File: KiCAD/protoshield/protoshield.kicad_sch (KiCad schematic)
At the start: 1 part, among them U2 Metro_ESP32S3

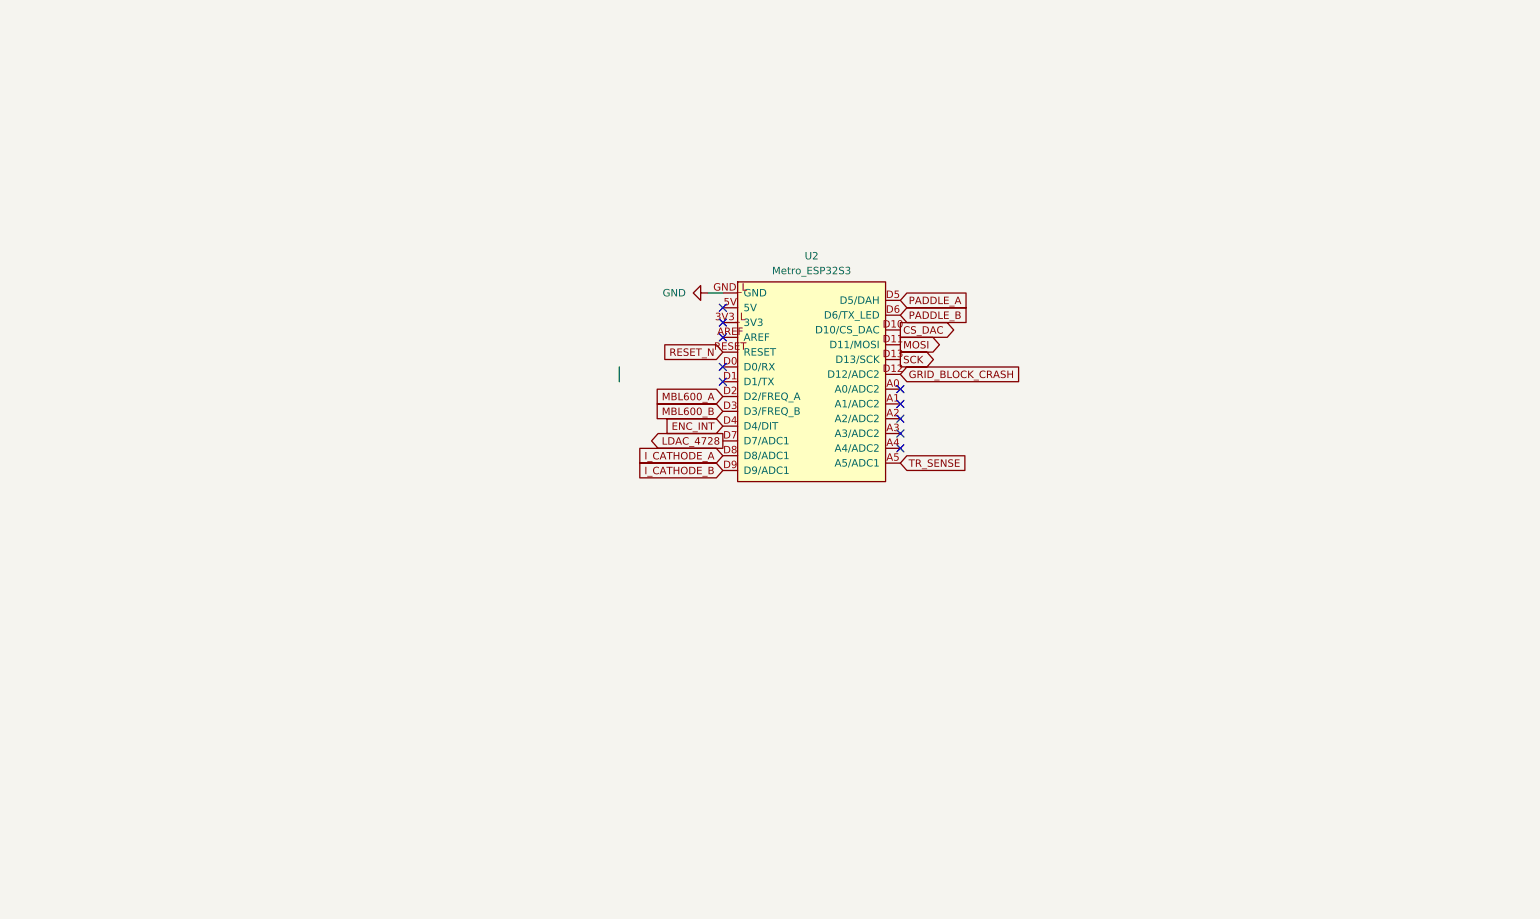
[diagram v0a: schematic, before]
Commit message: KiCad revB: protoshield schematic complete + 1N4728A symbol + misc board edits
Protoshield (Metro ESP32-S3 GPIO signal conditioning):
- Full schematic drawn: series R + bypass C + Zener clamp for I_CATHODE_A/B
  (1k+100nF+1N4728A), MBL600_A/B (10k/20k divider + 22pF), GRID_BLOCK_CRASH
  (1k+100nF), ENC_INT (330R+10k pull-up), PADDLE_A/B (10k pull-ups), RESET_N
  (100nF), TR_SENSE (10k pull-up), passthrough nodes for SPI and LDAC_4728
- All THT footprints assigned (ceramic disc caps, DIN0207 resistors, Phoenix
  MKDS-1.5 2-pin/3-pin terminal blocks)
- ENC_INT wiring gap fixed (R7 re-placed to connect J4 pin 2 to ENC_INT net)
- sym-lib-table added (points to shared xmitter.kicad_sym)
- protoshield.net generated netlist added for reference

Symbol library (xmitter.kicad_sym):
- Added 1N4728A (3.3V 1W Zener, DO-41) with correct KiCad 9.0 inline pts format

Other boards:
- analog/arduino.kicad_sch: minor junction/reference adjustments after Metro
  symbol was removed to protoshield in prior session
- bias: kicad_pro and kicad_sch updated (ongoing schematic work)
- power/sym-lib-table added for new stub project

Added: Purchase Orders (JLCPCB + Digi-Key invoices), tools/_scan_symbols.py

Co-Authored-By: Claude Sonnet 4.6 <noreply@anthropic.com>
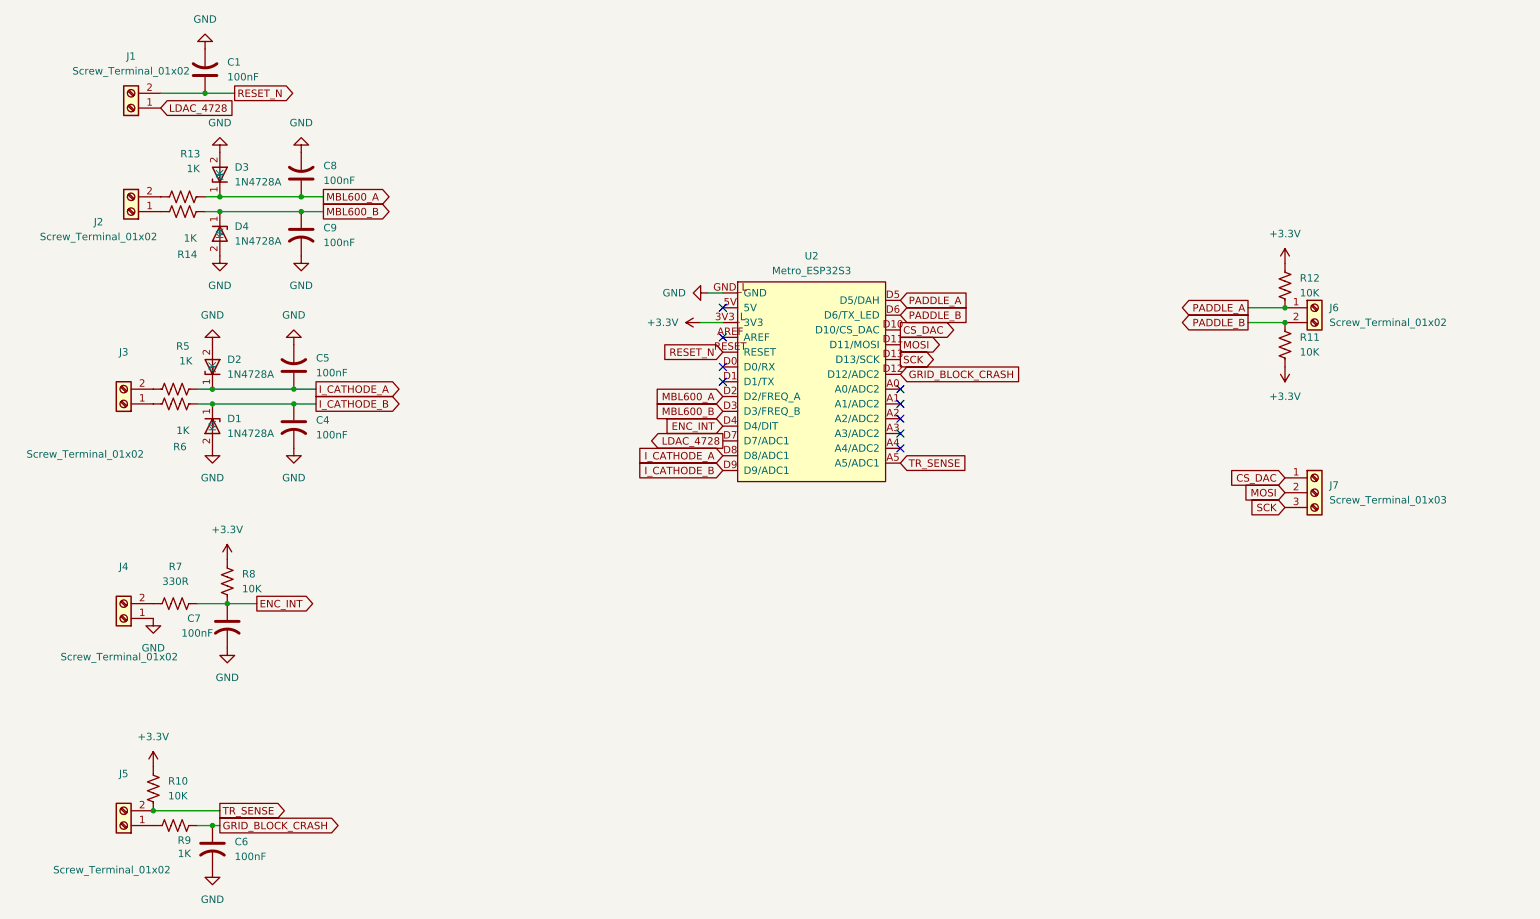
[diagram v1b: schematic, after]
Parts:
- added C1, C4, C5, C6, C7, C8, C9: 100nF, Capacitor_THT:C_Disc_D5.0mm_W2.5mm_P2.50mm, symbol Device:C_US
- added D1, D2, D3, D4: 1N4728A, Diode_THT:D_DO-41_SOD81_P10.16mm_Horizontal, symbol xmitter:1N4728A
- added J1, J2, J3, J4, J5, J6: Screw_Terminal_01x02, TerminalBlock_Phoenix:TerminalBlock_Phoenix_MKDS-1,5-2_1x02_P5.00mm_Horizontal, symbol Connector:Screw_Terminal_01x02
- added J7: Screw_Terminal_01x03, TerminalBlock_Phoenix:TerminalBlock_Phoenix_MKDS-1,5-3_1x03_P5.00mm_Horizontal, symbol Connector:Screw_Terminal_01x03
- added R10, R11, R12, R8: 10K, Resistor_THT:R_Axial_DIN0207_L6.3mm_D2.5mm_P10.16mm_Horizontal, symbol Device:R_US
- added R13, R14, R5, R6, R9: 1K, Resistor_THT:R_Axial_DIN0207_L6.3mm_D2.5mm_P10.16mm_Horizontal, symbol Device:R_US
- added R7: 330R, Resistor_THT:R_Axial_DIN0207_L6.3mm_D2.5mm_P10.16mm_Horizontal, symbol Device:R_US
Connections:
- net CS_DAC: now also J7.1 (Pin_1)
- net ENC_INT: now also C7.1, R7.2, R8.2
- net GND: now also C1.2, C4.2, C5.2, C6.2, C7.2, C8.2, C9.2, D1.2 (A), D2.2 (A), D3.2 (A), D4.2 (A), J4.1 (Pin_1)
- net GRID_BLOCK_CRASH: now also C6.1, R9.2
- net I_CATHODE_A: now also C5.1, D2.1 (K), R5.2
- net I_CATHODE_B: now also C4.1, D1.1 (K), R6.2
- net LDAC_4728: now also J1.1 (Pin_1)
- net MBL600_A: now also C8.1, D3.1 (K), R13.2
- net MBL600_B: now also C9.1, D4.1 (K), R14.2
- net MOSI: now also J7.2 (Pin_2)
- net PADDLE_A: now also J6.1 (Pin_1), R12.2
- net PADDLE_B: now also J6.2 (Pin_2), R11.1
- net RESET_N: now also C1.1, J1.2 (Pin_2)
- net SCK: now also J7.3 (Pin_3)
- net TR_SENSE: now also J5.2 (Pin_2), R10.2
- net +3.3V: now reaches U2.3V3_L (3V3)
- net +3.3V: now also R10.1, R11.2, R12.1, R8.1
- new net: J4.2 (Pin_2), R7.1
- new net: J2.2 (Pin_2), R13.1
- new net: J3.1 (Pin_1), R6.1
- new net: J3.2 (Pin_2), R5.1
- new net: J2.1 (Pin_1), R14.1
- new net: J5.1 (Pin_1), R9.1
- no-connect marks 10 -> 9

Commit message: KiCad revB: schematic review pass — I2C, ENC_INT, GND returns, GRID_BLOCK_CRASH clamp
Result of extended review pass against fresh netlists across all four
boards. All connectivity blockers resolved.

- Si5351 SDA/SCL wired via 0R jumpers (R8/R9) puts I2C on PCB traces
  for PCF8575 U17 and the RJ45 to the front panel. MCP4728 side has
  parallel 0R jumpers (R3/R4/R5) left DNP by default — STEMMA-QT is
  the intended path.
- ENC_INT chain unified end-to-end with staged names:
  ENC_INT_RAW (frontpanel encoder wire-OR) → ENC_INT_CLEAN (across
  CAT + analog pass-through) → ENC_INT_FINAL (post-protoshield
  conditioning). Frontpanel U4 (MCP1700-3.3 LDO) sources the +3.3V
  the pull-up R4 needs; pull-up moved to encoder side for sharper
  falling edges over the 2 m CAT run.
- Protoshield GRID_BLOCK_CRASH gets 1N4728A Zener clamp (D5),
  matching the I_CATHODE and MBL600 5V→3.3V clamp topology.
- Protoshield MBL600 conditioning rebuilt: 1K series + 100nF filter
  + 1N4728A clamp (was 10K/20K divider + 22pF that filtered nothing
  below RF).
- PADDLE_A/B and RESET_N removed from analog board — case-mounted
  switches wire directly to protoshield.
- Protoshield J1/J6 widened to 3-pin to include GND returns for the
  case-mounted paddle and reset switches.
- Bias board reference designators reorganized functionally
  (R_FA/R_FB feedback, R_GA/R_GB gain, R_PADA/R_PADB, R_GLA/R_GLB
  grid line, R_GATE, R_Z).
- New Documentation/control_board_functional_blocks.md captures
  KeyUp/Gate 2 keying, relay assignments (J6=T/R, J7=HV primary,
  J8=HV inrush), CD14538B heartbeat watchdog, TR_SENSE interlock,
  and J13 power-migration header.
- Fresh netlists exported for all four boards.

Co-Authored-By: Claude Opus 4.7 <noreply@anthropic.com>
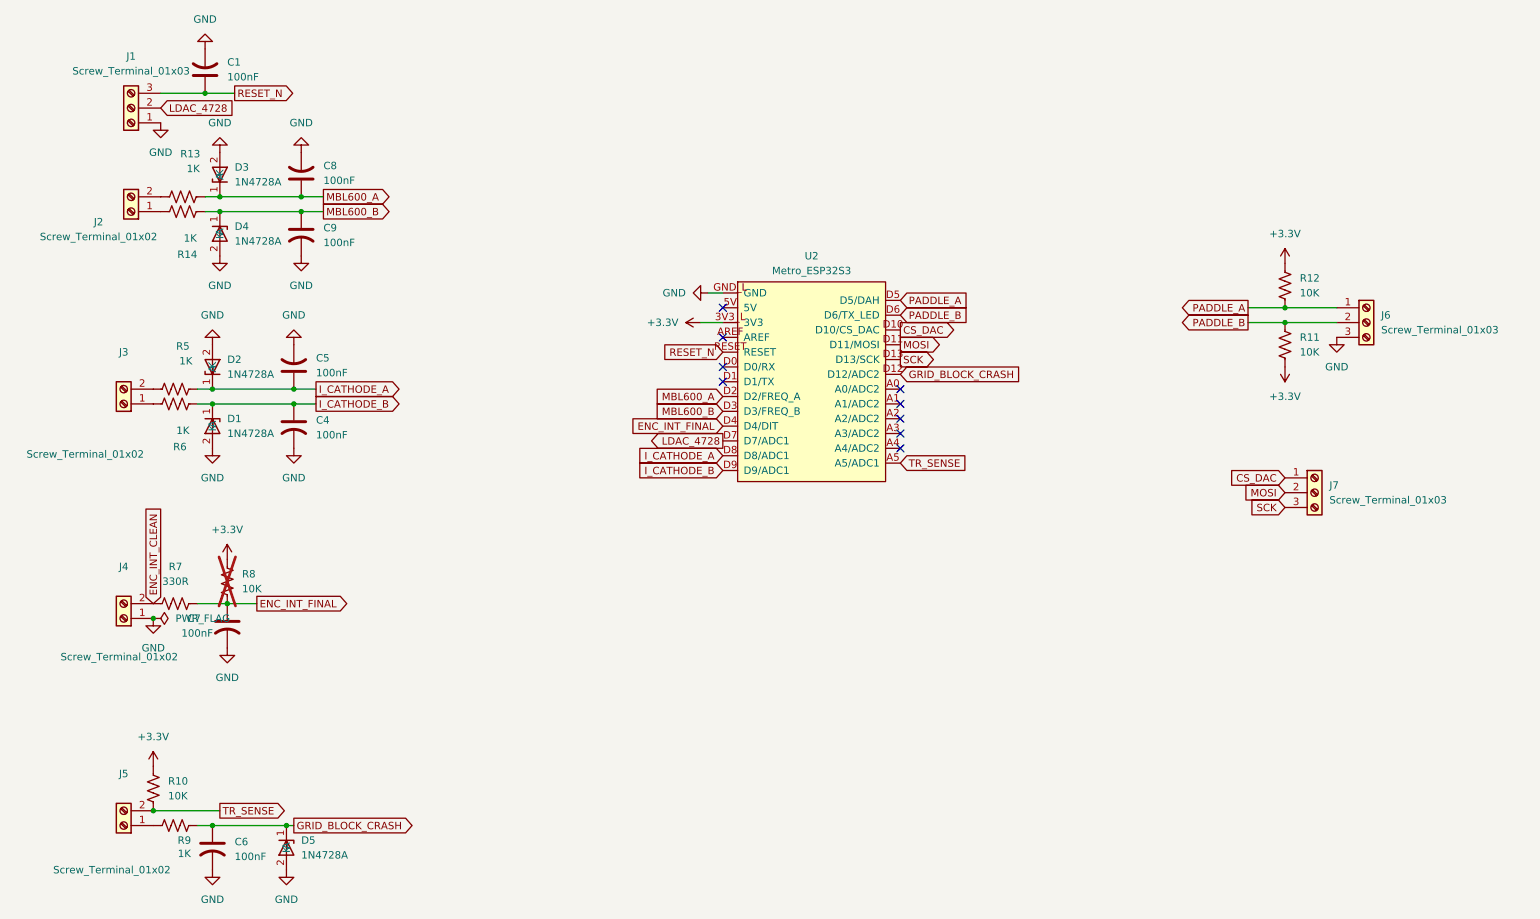
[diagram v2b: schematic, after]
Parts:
- removed J1, J6: Screw_Terminal_01x02, TerminalBlock_Phoenix:TerminalBlock_Phoenix_MKDS-1,5-2_1x02_P5.00mm_Horizontal, symbol Connector:Screw_Terminal_01x02
- added D5: 1N4728A, Diode_THT:D_DO-41_SOD81_P10.16mm_Horizontal, symbol xmitter:1N4728A
- added J1, J6: Screw_Terminal_01x03, symbol Connector:Screw_Terminal_01x03
- R8: now not fitted
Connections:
- net GND: now also D5.2 (A), J1.1 (Pin_1), J6.3 (Pin_3)
- net GRID_BLOCK_CRASH: now also D5.1 (K)
- net LDAC_4728: now also J1.2 (Pin_2)
- net PADDLE_A: now also J6.1 (Pin_1)
- net PADDLE_B: now also J6.2 (Pin_2)
- net RESET_N: now also J1.3 (Pin_3)
- net ENC_INT_CLEAN: now reaches J4.2 (Pin_2), R7.1
- net ENC_INT renamed ENC_INT_FINAL

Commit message: KiCad revB: assign 87 empty footprints via re-runnable scripts
Filled empty Footprint fields on capacitors, resistors, and screw
terminals across all four boards. All three scripts are re-runnable
and only fill empty fields (never overwrite existing assignments).

Scripts:
- assign_cap_footprints.py: extended CAP_LIB_IDS to also cover
  Device:C_US, Device:C_Polarized_US, Device:C_Small (was only
  Device:C and Device:C_Polarized). VALUE_TO_FOOTPRINT map unchanged.
- assign_connector_footprints.py (new): matches
  Connector:Screw_Terminal_01xNN to Phoenix MKDS-1,5-N horizontal
  P5.00mm per pin count (same pattern the protoshield already used).
- assign_resistor_footprints.py (new): matches Device:R and
  Device:R_US to the project-standard Resistor_THT:R_Axial_DIN0207
  L6.3mm_D2.5mm_P10.16mm_Horizontal footprint. All 46 populated
  resistors on the project already used this footprint; the empty
  ones now match.

Assignment counts:
- Capacitors: 42 (5 arduino, 33 vfo_complete, 2 bias, 2 frontpanel)
- Screw terminals: 17 (10 arduino, 4 bias, 1 frontpanel, 2 protoshield)
- Resistors: 28 (5 arduino, 21 vfo_complete, 2 frontpanel)

Deferred (need part-specific decisions, tracked in review notes):
- Coax connectors (12 total across analog + bias) - awaiting Cinch
  142-0701-201 footprint verification in KiCad's Connector_Coaxial
  library, or a custom footprint in xmitter.pretty/
- One-off ICs: F1 Polyfuse, U3 MCP4728, U21 LT1054
- 6 unmapped cap values in vfo_complete: 2pF x3, 220nF, 4700uF, 100uF
- U2 Metro_ESP32S3 (protoshield): intentionally empty (on_board no,
  plug-in module, not placed on PCB)

Also add three component datasheets: 1N4736AT-D (1N4728A family
reference), LM393-D, OPA1641.

Co-Authored-By: Claude Opus 4.7 <noreply@anthropic.com>
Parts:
- J1, J6: footprint (none) -> TerminalBlock_Phoenix:TerminalBlock_Phoenix_MKDS-1,5-3_1x03_P5.00mm_Horizontal
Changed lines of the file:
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@@
 			)
 		)
-		(property "Footprint" ""
+		(property "Footprint" "TerminalBlock_Phoenix:TerminalBlock_Phoenix_MKDS-1,5-3_1x03_P5.00mm_Horizontal"
 			(at 241.3 74.93 0)
 			(hide yes)
@@
 			)
 		)
-		(property "Footprint" ""
+		(property "Footprint" "TerminalBlock_Phoenix:TerminalBlock_Phoenix_MKDS-1,5-3_1x03_P5.00mm_Horizontal"
 			(at 29.21 38.1 0)
 			(hide yes)

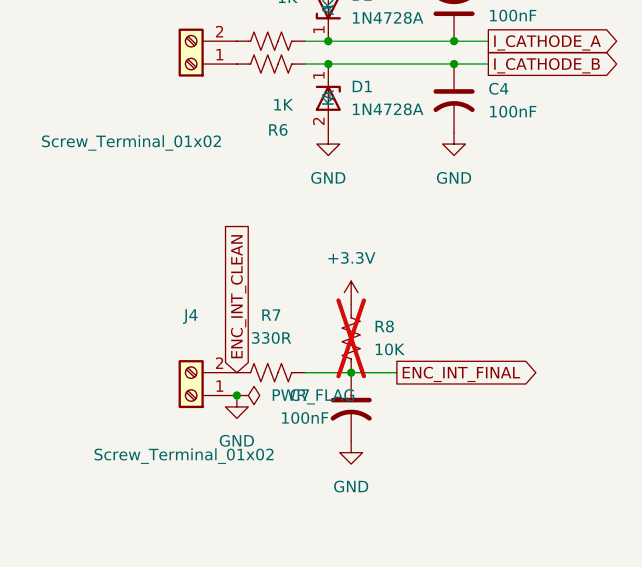
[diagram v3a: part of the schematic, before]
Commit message: KiCad revB: custom footprints, coax assignments, TO-92 widening, ENC_INT rewire
Second-pass footprint work: filled the remaining empty footprints
that couldn't be handled by the earlier stock-library scripts, added
custom footprints for parts KiCad's stock library doesn't cover, and
did a few schematic hygiene fixes surfaced during the deep-dive
reviews.

Custom footprints (new, xmitter.pretty/):
- SMA_Cinch_142-0701-201_Vertical_JackPCB - 50 Ohm SMA vertical
  through-hole jack for the analog board and bias board coax
  interconnects (I_CATHODE, GRID_CTL, GRID_BLOCK_CRASH, GRID_BIAS).
  Center pin 1.57 mm hole + 4 ground tabs on a 5.08 mm square
  pattern. All 4 ground tabs share pin number 2 (shield).
- CP_Radial_Kemet_ESK_D22.0mm_P10.00mm - Kemet ESK case Q4 radial
  electrolytic (22 mm dia, 10 mm pitch) for C72 = 4700 uF 50V.
- Fuse_Littelfuse_60R_L7.9mm_W3.1mm_P5.08mm - Littelfuse 60R Series
  radial polyfuse for F1 = 60R050XU (0.5 A hold). Body sized for the
  small-body variants (010X-090X); pitch 5.08 mm, drill 0.7 mm.
- C_Axial_Kemet_Aximax_C41X_L4.5mm_D2.6mm_P7.62mm_Horizontal - Kemet
  Aximax C410 axial C0G ceramic for the three 2 pF caps
  (C69/C70/C71) in the vfo_complete keyer chain. Horizontal mount,
  7.62 mm pitch.

New re-runnable script:
- tools/assign_coax_footprints.py - maps
  Connector:Conn_Coaxial_Small symbols to the new Cinch SMA
  footprint. Same "only fill empty, never overwrite" pattern as the
  existing assign_*_footprints.py scripts.

Script extension:
- tools/assign_cap_footprints.py - added value entries for 4700uF
  (Kemet ESK), 220nF (D6 disc), 2pF (Kemet Aximax C41X), and 100uF
  (Vishay 036 RSP). All four entries include the datasheet path and
  the specific case-size rationale.

Schematic edits (all boards):
- 12 coax connectors assigned to the new Cinch SMA footprint
  (analog J17-J19/J23-J24, bias J1/J2/J4/J6/J9/J10/J12) via the new
  assign_coax script.
- 5 caps in vfo_complete assigned via extended assign_cap_footprints
  (C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
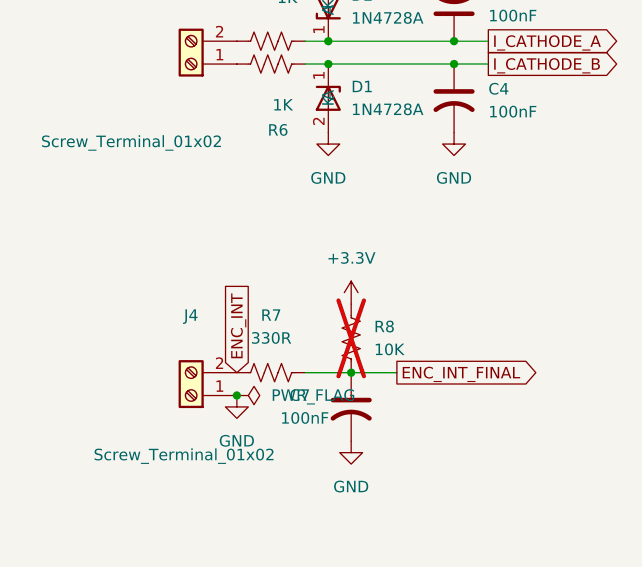
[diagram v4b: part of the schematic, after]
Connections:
- net ENC_INT_CLEAN renamed ENC_INT
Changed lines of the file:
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@@
 		)
 	)
-	(global_label "ENC_INT_CLEAN"
+	(global_label "ENC_INT"
 		(shape input)
 		(at 33.02 123.19 90)
